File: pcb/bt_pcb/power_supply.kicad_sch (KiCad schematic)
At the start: 24 parts, among them IC1 LTC3621EMS8E-25#PBF, J1 Conn_01x02, J2 694106301002, J3 Conn_01x01, U1 TLV76133DCY, U2 TLV76133DCY

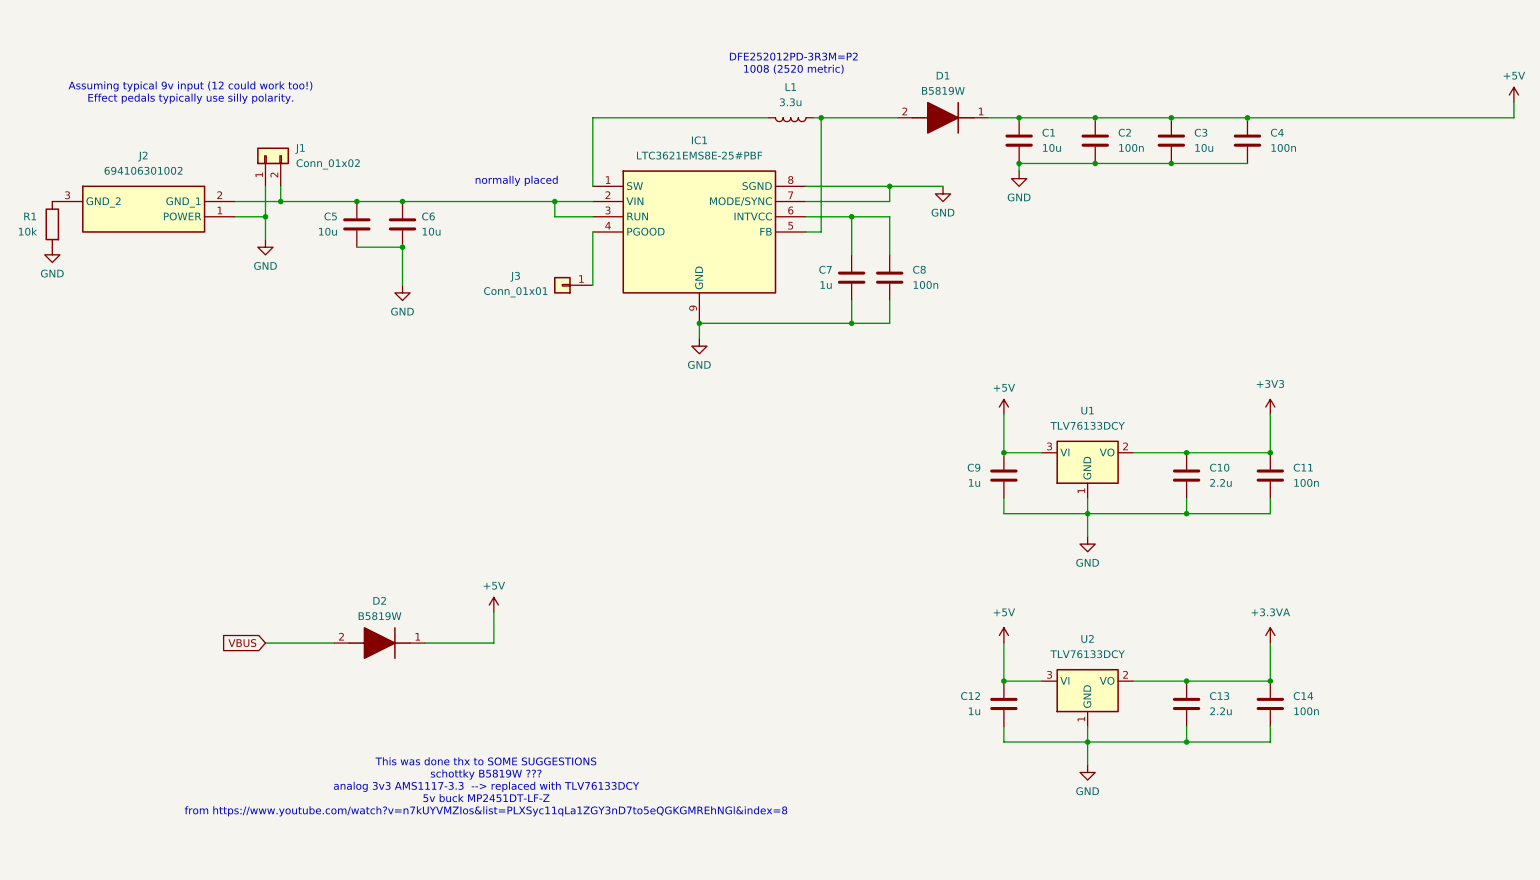
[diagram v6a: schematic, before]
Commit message: redo of power supply
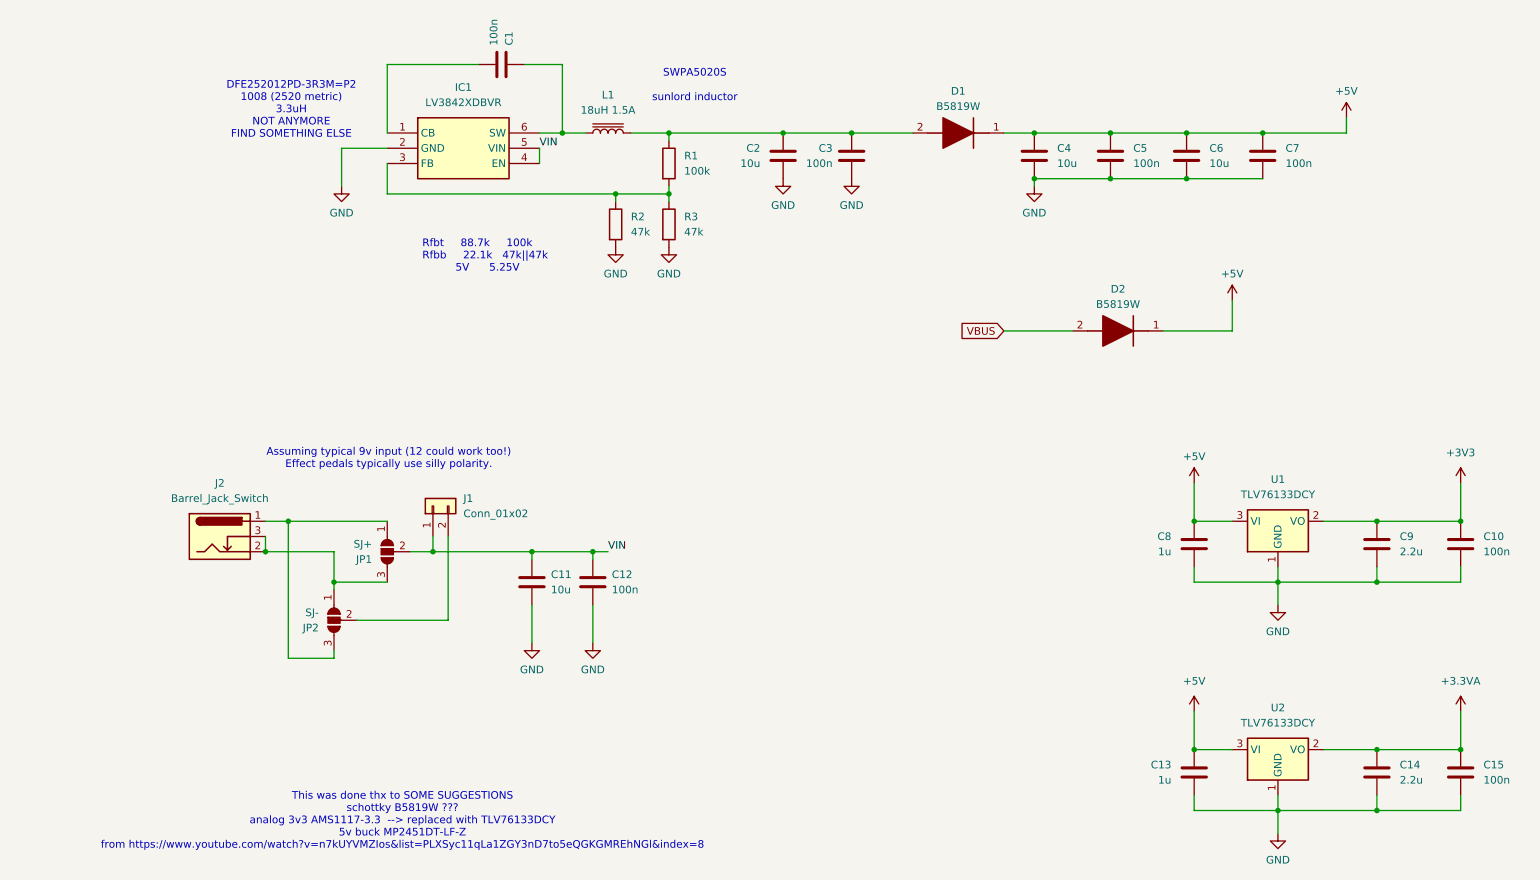
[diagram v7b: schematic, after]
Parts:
- removed C5: 10u, Capacitor_SMD:C_0805_2012Metric_Pad1.18x1.45mm_HandSolder, symbol Device:C
- removed C7: 1u, Capacitor_SMD:C_0603_1608Metric_Pad1.08x0.95mm_HandSolder, symbol Device:C
- removed C8: 100n, Capacitor_SMD:C_0603_1608Metric_Pad1.08x0.95mm_HandSolder, symbol Device:C
- removed IC1: LTC3621EMS8E-25#PBF, library:SOP65P490X110-9N, symbol library:LTC3621EMS8E-25#PBF
- removed J2: 694106301002, library:694106301002_1, symbol library:694106301002
- removed J3: Conn_01x01, Connector_PinHeader_2.54mm:PinHeader_1x01_P2.54mm_Vertical, symbol Connector_Generic:Conn_01x01
- removed L1: 3.3u, Inductor_SMD:L_1008_2520Metric_Pad1.43x2.20mm_HandSolder, symbol Device:L
- added C1, C12, C3: 100n, Capacitor_SMD:C_0603_1608Metric_Pad1.08x0.95mm_HandSolder, symbol Device:C
- added C2: 10u, Capacitor_SMD:C_0805_2012Metric_Pad1.18x1.45mm_HandSolder, symbol Device:C
- added IC1: LV3842XDBVR, library:SOT95P280X145-6N, symbol library:LV3842XDBVR
- added J2: Barrel_Jack_Switch, library:694106301002_1, symbol Connector:Barrel_Jack_Switch
- added JP1: SJ+, Jumper:SolderJumper-3_P1.3mm_Open_Pad1.0x1.5mm, symbol Jumper:SolderJumper_3_Open
- added JP2: SJ-, Jumper:SolderJumper-3_P1.3mm_Open_Pad1.0x1.5mm, symbol Jumper:SolderJumper_3_Open
- added L1: 18uH 1.5A, symbol Device:L_Iron
- added R2, R3: 47k, Resistor_SMD:R_0603_1608Metric_Pad0.98x0.95mm_HandSolder, symbol Device:R
- R1: value 10k -> 100k
- renumbered C11 to C10, C6 to C11, C12 to C13, C13 to C14, C14 to C15, C1 to C4, C2 to C5, C3 to C6, C4 to C7, C9 to C8, C10 to C9
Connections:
- net GND: now also C12.2, C2.2, C3.2, IC1.2 (GND), R2.2, R3.2; no longer J1.1 (Pin_1), R1.2
- net at D1.2 (A): now also R1.1, C2.1, C3.1, L1.2
- net at J1.2 (Pin_2): now also JP2.2 (C); no longer C11.1
- new net: J2.1, JP1.1 (A), JP2.3 (B)
- new net: J2.2, J2.3, JP1.3 (B), JP2.1 (A)
- new net: IC1.3 (FB), R1.2, R2.1, R3.1
- new net: C1.1, IC1.6 (SW), L1.1
- new net: C1.2, IC1.1 (CB)
- new net VIN: C11.1, C12.1, IC1.4 (EN), IC1.5 (VIN), J1.1 (Pin_1), JP1.2 (C)
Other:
- note added: "DFE252012PD-3R3M=P2 1008 (2520 metric) 3.3uH NOT ANYMORE FIND SOMETHING ELSE"
- note added: "Rfbt 88.7k 100k Rfbb 22.1k 47k||47k 5V 5.25V"
- note added: "SWPA5020S sunlord inductor"
- note removed: "DFE252012PD-3R3M=P2 1008 (2520 metric)"
- note removed: "normally placed"
- moved on the sheet: C10, C11, C13, C14, C15, C4, C5, C6, C7, C8, C9, D1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

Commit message: made a bom
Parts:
- J1: now left out of the parts list
- L1: footprint (none) -> library:SRR6040A180M
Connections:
- net GND: now also J1.1 (Pin_1), JP2.2 (C)
- net VIN: now also J1.2 (Pin_2); no longer J1.1 (Pin_1)
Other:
- moved on the sheet: J1
